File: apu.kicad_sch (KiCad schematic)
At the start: 15 parts, among them J3 Conn_01x02

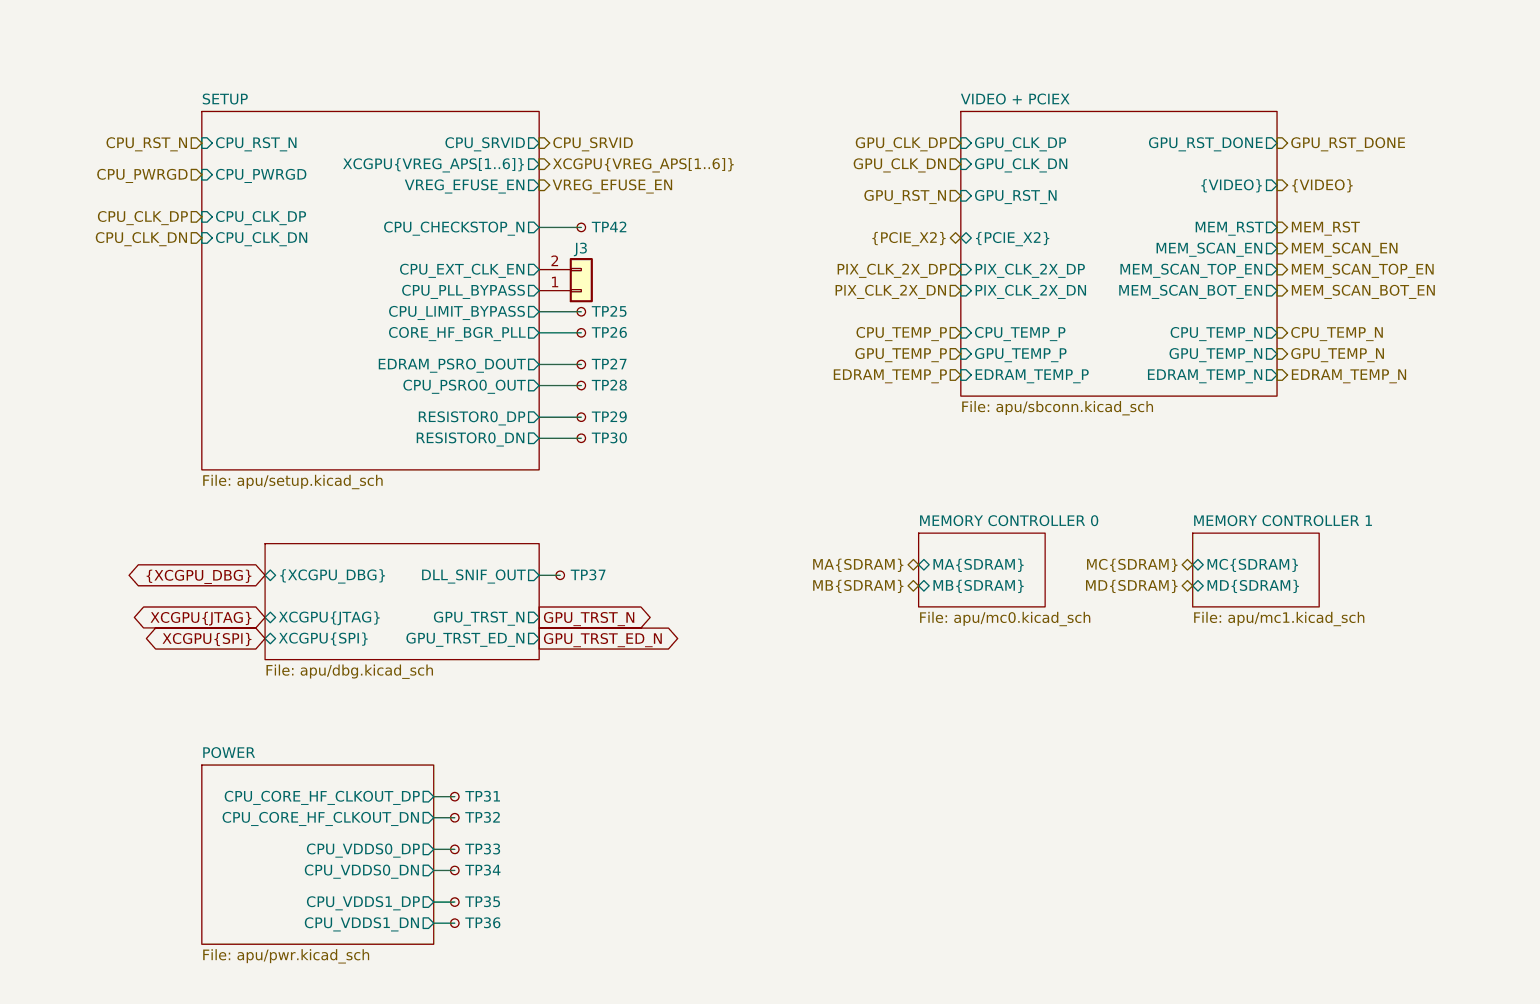
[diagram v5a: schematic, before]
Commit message: Multipurpose and standby power rails, Reannotated schematic
Added V_1P2, V_1P8, V_5P0DUAL, V_EFUSE, V_GPUPCIE, V_3P3STBY and V_1P2STBY
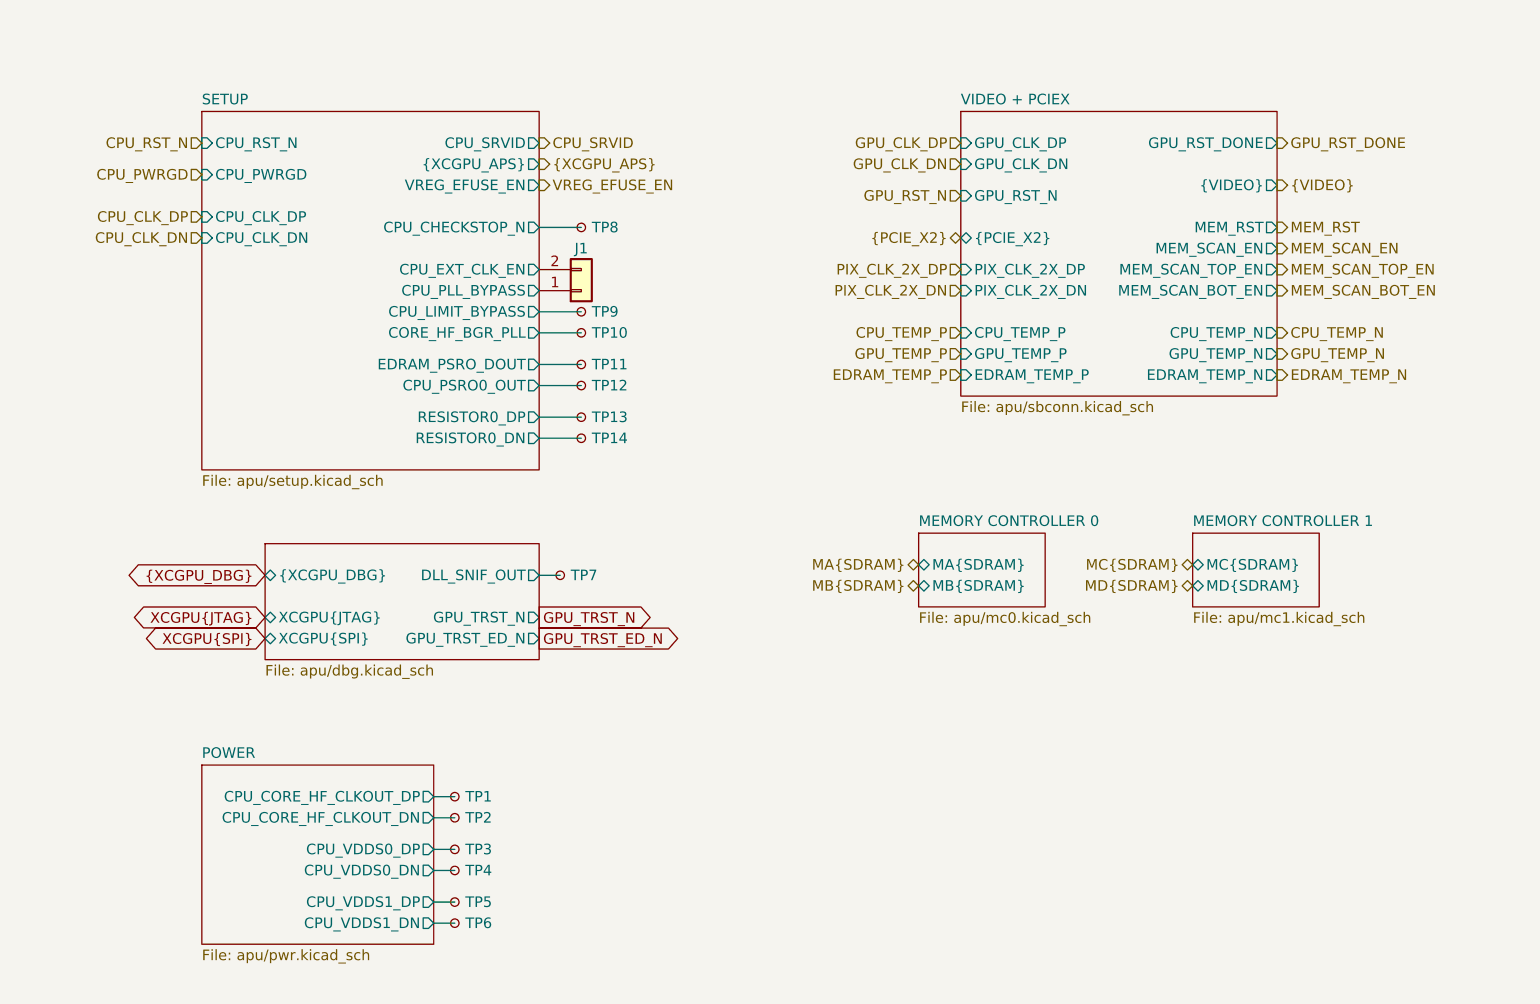
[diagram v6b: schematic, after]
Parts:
- renumbered J3 to J1, TP31 to TP1, TP26 to TP10, TP27 to TP11, TP28 to TP12, TP29 to TP13, TP30 to TP14, TP32 to TP2, TP33 to TP3, TP34 to TP4, TP35 to TP5, TP36 to TP6, TP37 to TP7, TP42 to TP8, TP25 to TP9
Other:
- sheet SETUP ports: added {XCGPU_APS}; removed XCGPU{VREG_APS[1..6]}
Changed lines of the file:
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@@
+		)
+	)
+	(hierarchical_label "{XCGPU_APS}"
+		(shape output)
+		(at 74.93 33.02 0)
+		(effects
+			(font
+				(size 1.27 1.27)
+			)
+			(justify left)
 		)
 	)
@@
 			)
 			(justify right)
-		)
-	)
-	(hierarchical_label "XCGPU{VREG_APS[1..6]}"
-		(shape output)
-		(at 74.93 33.02 0)
-		(effects
-			(font
-				(size 1.27 1.27)
-			)
-			(justify left)
 		)
 	)
@@
 		(on_board yes)
 		(dnp no)
-		(property "Reference" "TP33"
+		(property "Reference" "TP3"
 			(at 66.04 115.57 0)
 			(effects
@@
 			(project "Mantaray"
 				(path "/16640ecb-e4a4-4594-871b-70047bfba6e0/15d9acf0-ed9b-44aa-a266-2c44722c6abb"
-					(reference "TP33")
+					(reference "TP3")
 					(unit 1)
 				)
@@
 		(on_board yes)
 		(dnp no)
-		(property "Reference" "J3"
+		(property "Reference" "J1"
 			(at 80.01 43.18 0)
 			(effects
@@
 			(project "Mantaray"
 				(path "/16640ecb-e4a4-4594-871b-70047bfba6e0/15d9acf0-ed9b-44aa-a266-2c44722c6abb"
-					(reference "J3")
+					(reference "J1")
 					(unit 1)
 				)
@@
 		(on_board yes)
 		(dnp no)
-		(property "Reference" "TP29"
+		(property "Reference" "TP13"
 			(at 81.28 63.5 0)
 			(effects
@@
 			(project "Mantaray"
 				(path "/16640ecb-e4a4-4594-871b-70047bfba6e0/15d9acf0-ed9b-44aa-a266-2c44722c6abb"
-					(reference "TP29")
+					(reference "TP13")
 					(unit 1)
 				)
@@
 		(on_board yes)
 		(dnp no)
-		(property "Reference" "TP30"
+		(property "Reference" "TP14"
 			(at 81.28 66.04 0)
 			(effects
@@
 			(project "Mantaray"
 				(path "/16640ecb-e4a4-4594-871b-70047bfba6e0/15d9acf0-ed9b-44aa-a266-2c44722c6abb"
-					(reference "TP30")
+					(reference "TP14")
 					(unit 1)
 				)
@@
 		(on_board yes)
 		(dnp no)
-		(property "Reference" "TP31"
+		(property "Reference" "TP1"
 			(at 66.04 109.22 0)
 			(effects
@@
 			(project "Mantaray"
 				(path "/16640ecb-e4a4-4594-871b-70047bfba6e0/15d9acf0-ed9b-44aa-a266-2c44722c6abb"
-					(reference "TP31")
+					(reference "TP1")
 					(unit 1)
 				)
@@
 		(on_board yes)
 		(dnp no)
-		(property "Reference" "TP36"
+		(property "Reference" "TP6"
 			(at 66.04 124.46 0)
 			(effects
@@
 			(project "Mantaray"
 				(path "/16640ecb-e4a4-4594-871b-70047bfba6e0/15d9acf0-ed9b-44aa-a266-2c44722c6abb"
-					(reference "TP36")
+					(reference "TP6")
 					(unit 1)
 				)
@@
 		(on_board yes)
 		(dnp no)
-		(property "Reference" "TP28"
+		(property "Reference" "TP12"
 			(at 81.28 59.69 0)
 			(effects
@@
 			(project "Mantaray"
 				(path "/16640ecb-e4a4-4594-871b-70047bfba6e0/15d9acf0-ed9b-44aa-a266-2c44722c6abb"
-					(reference "TP28")
+					(reference "TP12")
 					(unit 1)
 				)
@@
 		(on_board yes)
 		(dnp no)
-		(property "Reference" "TP35"
+		(property "Reference" "TP5"
 			(at 66.04 121.92 0)
 			(effects
@@
 			(project "Mantaray"
 				(path "/16640ecb-e4a4-4594-871b-70047bfba6e0/15d9acf0-ed9b-44aa-a266-2c44722c6abb"
-					(reference "TP35")
+					(reference "TP5")
 					(unit 1)
 				)
@@
 		(on_board yes)
 		(dnp no)
-		(property "Reference" "TP25"
+		(property "Reference" "TP9"
 			(at 81.28 50.8 0)
 			(effects
@@
 			(project "Mantaray"
 				(path "/16640ecb-e4a4-4594-871b-70047bfba6e0/15d9acf0-ed9b-44aa-a266-2c44722c6abb"
-					(reference "TP25")
+					(reference "TP9")
 					(unit 1)
 				)
@@
 		(on_board yes)
 		(dnp no)
-		(property "Reference" "TP26"
+		(property "Reference" "TP10"
 			(at 81.28 53.34 0)
 			(effects
@@
 			(project "Mantaray"
 				(path "/16640ecb-e4a4-4594-871b-70047bfba6e0/15d9acf0-ed9b-44aa-a266-2c44722c6abb"
-					(reference "TP26")
+					(reference "TP10")
 					(unit 1)
 				)
@@
 		(on_board yes)
 		(dnp no)
-		(property "Reference" "TP42"
+		(property "Reference" "TP8"
 			(at 81.28 40.64 0)
 			(effects
@@
 			(project "Mantaray"
 				(path "/16640ecb-e4a4-4594-871b-70047bfba6e0/15d9acf0-ed9b-44aa-a266-2c44722c6abb"
-					(reference "TP42")
+					(reference "TP8")
 					(unit 1)
 				)
@@
 		(on_board yes)
 		(dnp no)
-		(property "Reference" "TP32"
+		(property "Reference" "TP2"
 			(at 66.04 111.76 0)
 			(effects
@@
 			(project "Mantaray"
 				(path "/16640ecb-e4a4-4594-871b-70047bfba6e0/15d9acf0-ed9b-44aa-a266-2c44722c6abb"
-					(reference "TP32")
+					(reference "TP2")
 					(unit 1)
 				)
@@
 		(on_board yes)
 		(dnp no)
-		(property "Reference" "TP37"
+		(property "Reference" "TP7"
 			(at 78.74 82.55 0)
 			(effects
@@
 			(project "Mantaray"
 				(path "/16640ecb-e4a4-4594-871b-70047bfba6e0/15d9acf0-ed9b-44aa-a266-2c44722c6abb"
-					(reference "TP37")
+					(reference "TP7")
 					(unit 1)
 				)
@@
 		(on_board yes)
 		(dnp no)
-		(property "Reference" "TP27"
+		(property "Reference" "TP11"
 			(at 81.28 57.15 0)
 			(effects
@@
 			(project "Mantaray"
 				(path "/16640ecb-e4a4-4594-871b-70047bfba6e0/15d9acf0-ed9b-44aa-a266-2c44722c6abb"
-					(reference "TP27")
+					(reference "TP11")
 					(unit 1)
 				)
@@
 		(on_board yes)
 		(dnp no)
-		(property "Reference" "TP34"
+		(property "Reference" "TP4"
 			(at 66.04 118.11 0)
 			(effects
@@
 			(project "Mantaray"
 				(path "/16640ecb-e4a4-4594-871b-70047bfba6e0/15d9acf0-ed9b-44aa-a266-2c44722c6abb"
-					(reference "TP34")
+					(reference "TP4")
 					(unit 1)
 				)
@@
 			)
 		)
-		(pin "XCGPU{VREG_APS[1..6]}" output
+		(pin "{XCGPU_APS}" output
 			(at 74.93 33.02 0)
 			(effects
